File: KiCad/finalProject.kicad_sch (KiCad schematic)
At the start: 19 parts, among them U1 MCP601-xP, U2 MCP601-xP

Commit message: update schematic
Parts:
- added SW1: SW_DIP_x01, symbol Switch:SW_DIP_x01
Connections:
- net GND: now also SW1.1
- new net P34: SW1.2
- no-connect marks 0 -> 1
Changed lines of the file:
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@@
 		(color 0 0 0 0)
 	)
+	(no_connect
+		(at 31.75 66.04)
+	)
 	(wire
 		(pts
@@
 	(wire
 		(pts
+			(xy 90.17 93.98) (xy 90.17 95.25)
+		)
+		(stroke
+			(width 0)
+			(type default)
+		)
+	)
+	(wire
+		(pts
 			(xy 135.89 104.14) (xy 135.89 106.68)
 		)
@@
 	(wire
 		(pts
+			(xy 58.42 93.98) (xy 58.42 88.9)
+		)
+		(stroke
+			(width 0)
+			(type default)
+		)
+	)
+	(wire
+		(pts
 			(xy 227.33 113.03) (xy 229.87 113.03)
 		)
@@
 	(wire
 		(pts
+			(xy 74.93 93.98) (xy 58.42 93.98)
+		)
+		(stroke
+			(width 0)
+			(type default)
+		)
+	)
+	(wire
+		(pts
 			(xy 129.54 34.29) (xy 129.54 41.91)
 		)
@@
 	(wire
 		(pts
-			(xy 26.67 66.04) (xy 39.37 66.04)
+			(xy 31.75 66.04) (xy 39.37 66.04)
 		)
 		(stroke
@@
 		)
 	)
-	(label "SCK"
+	(label "SCLK"
 		(at 26.67 60.96 0)
 		(fields_autoplaced yes)
@@
 		)
 	)
+	(label "P34"
+		(at 58.42 88.9 0)
+		(fields_autoplaced yes)
+		(effects
+			(font
+				(size 1.27 1.27)
+			)
+			(justify left bottom)
+		)
+	)
 	(label "d6"
 		(at 72.39 63.5 0)
@@
 		)
 	)
-	(label "CIPO"
-		(at 26.67 66.04 0)
-		(fields_autoplaced yes)
-		(effects
-			(font
-				(size 1.27 1.27)
-			)
-			(justify left bottom)
-		)
-	)
 	(label "GND"
 		(at 60.96 50.8 0)
@@
 		)
 	)
+	(label "reset"
+		(at 60.96 93.98 0)
+		(fields_autoplaced yes)
+		(effects
+			(font
+				(size 1.27 1.27)
+			)
+			(justify left bottom)
+		)
+	)
 	(label "d1"
 		(at 125.73 41.91 0)
@@
 	)
 	(symbol
+		(lib_id "Switch:SW_DIP_x01")
+		(at 82.55 93.98 180)
+		(unit 1)
+		(exclude_from_sim no)
+		(in_bom yes)
+		(on_board yes)
+		(dnp no)
+		(fields_autoplaced yes)
+		(property "Reference" "SW1"
+			(at 82.55 86.36 0)
+			(effects
+				(font
+					(size 1.27 1.27)
+				)
+			)
+		)
+		(property "Value" "SW_DIP_x01"
+			(at 82.55 88.9 0)
+			(effects
+				(font
+					(size 1.27 1.27)
+				)
+			)
+		)
+		(property "Footprint" ""
+			(at 82.55 93.98 0)
+			(effects
+				(font
+					(size 1.27 1.27)
+				)
+				(hide yes)
+			)
+		)
+		(property "Datasheet" "~"
+			(at 82.55 93.98 0)
+			(effects
+				(font
+					(size 1.27 1.27)
+				)
+				(hide yes)
+			)
+		)
+		(property "Description" "1x DIP Switch, Single Pole Single Throw (SPST) switch, small symbol"
+			(at 82.55 93.98 0)
+			(effects
+				(font
+					(size 1.27 1.27)
+				)
+				(hide yes)
+			)
+		)
+		(pin "2"
+		)
+		(pin "1"
+		)
+		(instances
+			(project ""
+				(path "/86aea3a1-09bf-48eb-af77-bb5f50a3b6b5"
+					(reference "SW1")
+					(unit 1)
+				)
+			)
+		)
+	)
+	(symbol
 		(lib_id "Device:R_US")
 		(at 139.7 165.1 0)
@@
 					(unit 1)
 				)
+			)
+		)
+	)
+	(symbol
+		(lib_id "power:GND")
+		(at 90.17 95.25 0)
+		(unit 1)
+		(exclude_from_sim no)
+		(in_bom yes)
+		(on_board yes)
+		(dnp no)
+		(fields_autoplaced yes)
+		(property "Reference" "#PWR012"
+			(at 90.17 101.6 0)
+			(effects
+				(font
+					(size 1.27 1.27)
+				)
+				(hide yes)
+			)
+		)
+		(property "Value" "GND"
+			(at 90.17 100.33 0)
+			(effects
+				(font
+					(size 1.27 1.27)
+				)
+			)
+		)
+		(property "Footprint" ""
+			(at 90.17 95.25 0)
+			(effects
+				(font
+					(size 1.27 1.27)
+				)
+				(hide yes)
+			)
+		)
+		(property "Datasheet" ""
+			(at 90.17 95.25 0)
+			(effects
+				(font
+					(size 1.27 1.27)
+				)
+				(hide yes)
+			)
+		)
+		(property "Description" "Power symbol creates a global label with name \"GND\" , ground"
+			(at 90.17 95.25 0)
+			(effects
+				(font
+					(size 1.27 1.27)
+				)
+				(hide yes)
+			)
+		)
+		(pin "1"
+		)
+		(instances
+			(project ""
+				(path "/86aea3a1-09bf-48eb-af77-bb5f50a3b6b5"
+					(reference "#PWR012")
+					(unit 1)
+				)

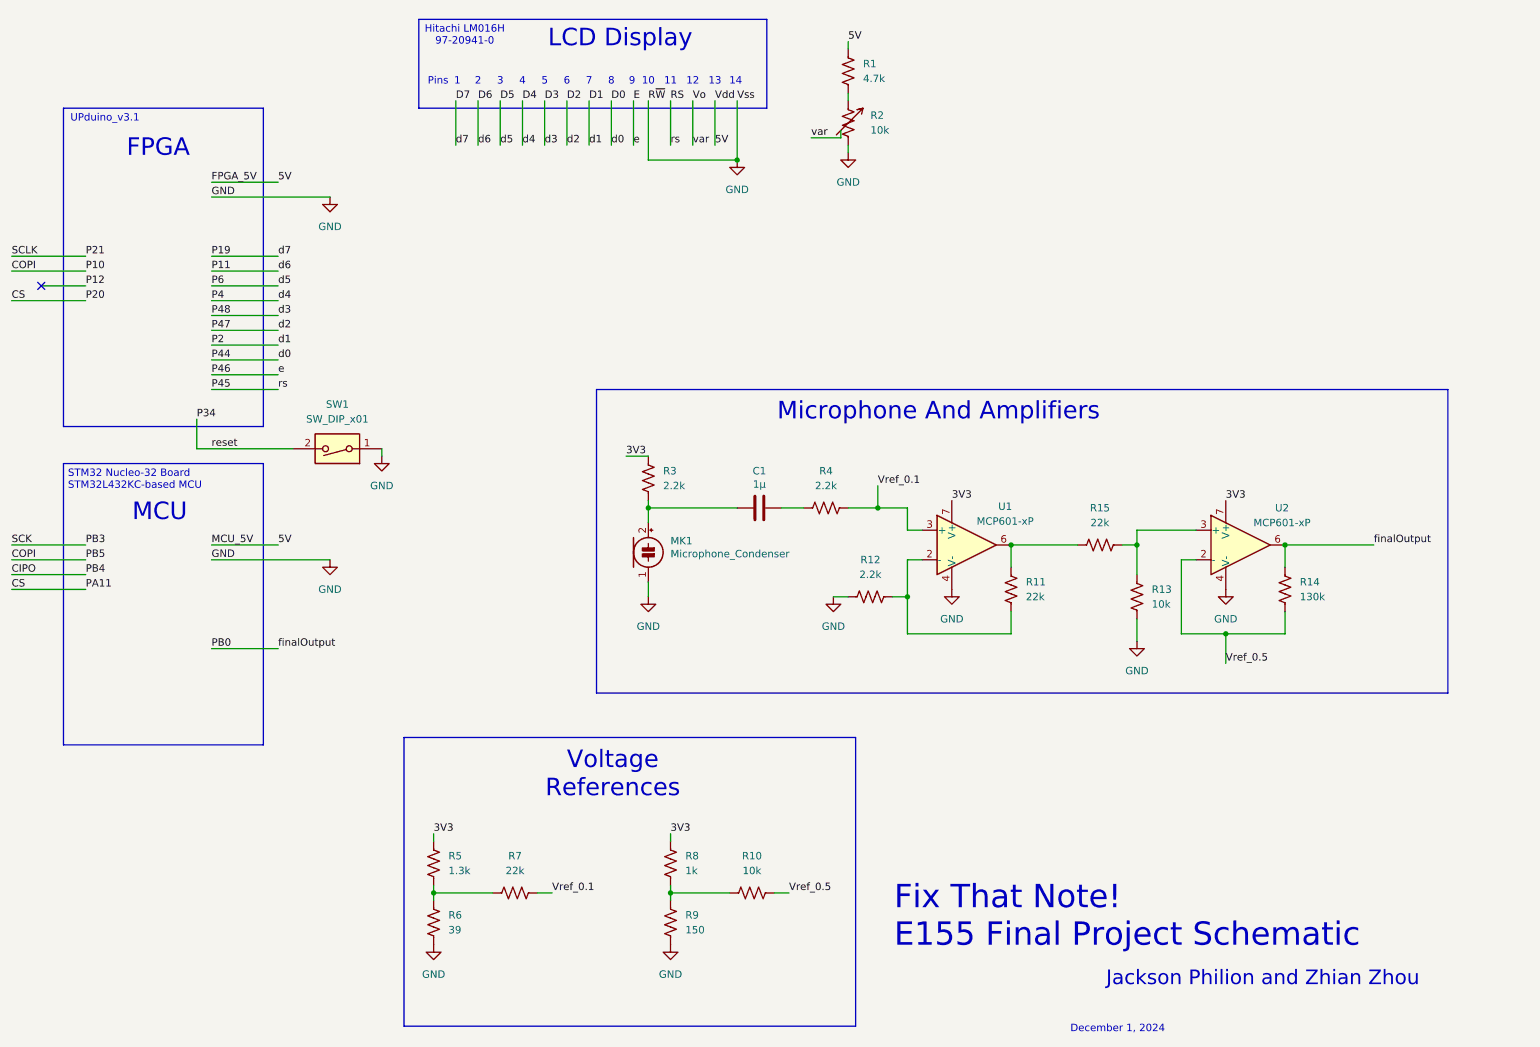
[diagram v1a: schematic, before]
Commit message: schematic update
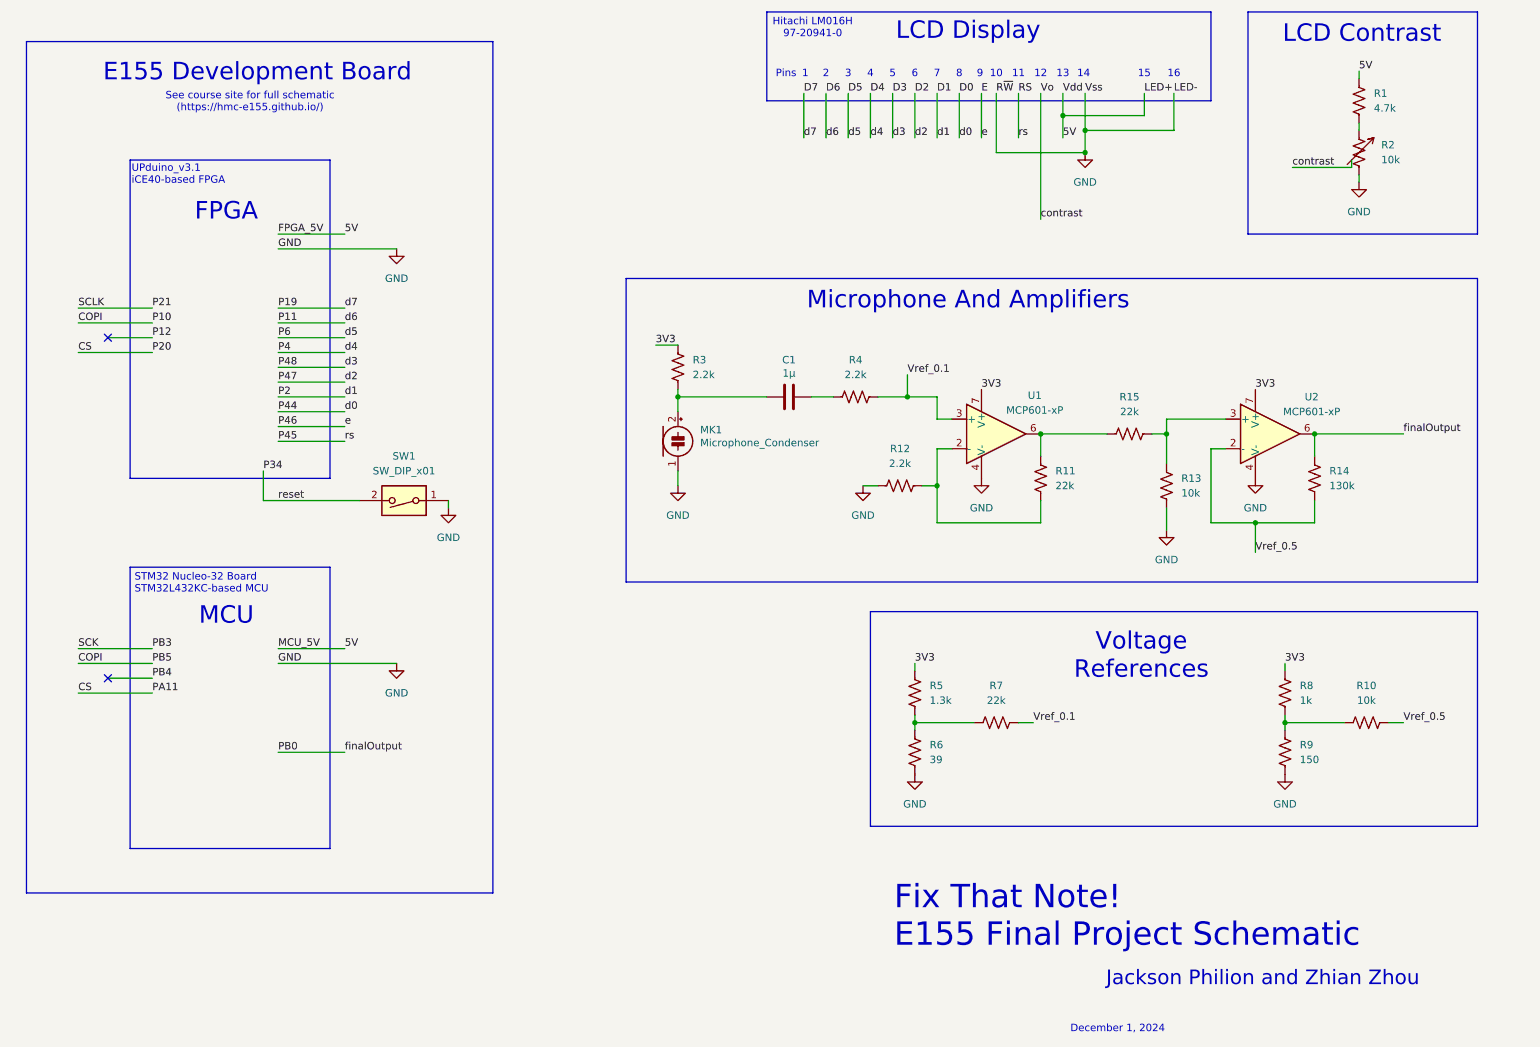
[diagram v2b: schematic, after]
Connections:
- no-connect marks 1 -> 2
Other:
- note added: "15"
- note added: "16"
- note added: "E155 Development Board"
- note added: "LCD Contrast"
- note added: "See course site for full schematic (https://hmc-e155.github.io/)"
- note added: "UPduino_v3.1 iCE40-based FPGA"
- note removed: "UPduino_v3.1"
- moved on the sheet: C1, MK1, R1, R10, R11, R12, R13, R14, R15, R2, R3, R4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
